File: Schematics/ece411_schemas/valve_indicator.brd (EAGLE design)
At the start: 85.1 x 53.6 mm, 66 parts, among them IC1 STM32F042K6T6, T1 2N2222, T2 2N2222, T3 2N2222, T4 2N2222, U1 DIODES_INC._AZ34063UMTR-G1DIO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, U2 DIODES_INC._AZ34063UMTR-G1DIO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

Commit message: dru added, added attributes
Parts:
- RS_L: device SparkFun-Resistors:0603 -> rcl:R0603
- moved C1_H 10.8 mm to (29.2, 34.9), turned to 180 degrees
- moved RS_L 3.59 mm to (36.8, 29.8)
- moved U2 1.42 mm to (34.9, 40.6)
- moved U1 1.42 mm to (34.9, 34.3)
- moved R1_H 0.63 mm to (40.6, 36.8)
- moved R2_H 0.63 mm to (44.5, 38.7)
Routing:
- net +3V3: track 66.0 -> 71.7 mm
- net N$21: track 50.2 -> 47.4 mm
- net N$17: track 59.3 -> 56.9 mm
- net N$18: track 10.9 -> 8.90 mm
- net N$2: track 10.8 -> 8.91 mm
- net N$1: track 54.5 -> 52.9 mm
- net GND: track 52.7 -> 51.7 mm
- net N$13: track 87.6 -> 86.9 mm
- net N$12: track 46.3 -> 45.5 mm
- net N$11: track 51.1 -> 50.3 mm
- net N$19: track 6.97 -> 6.33 mm

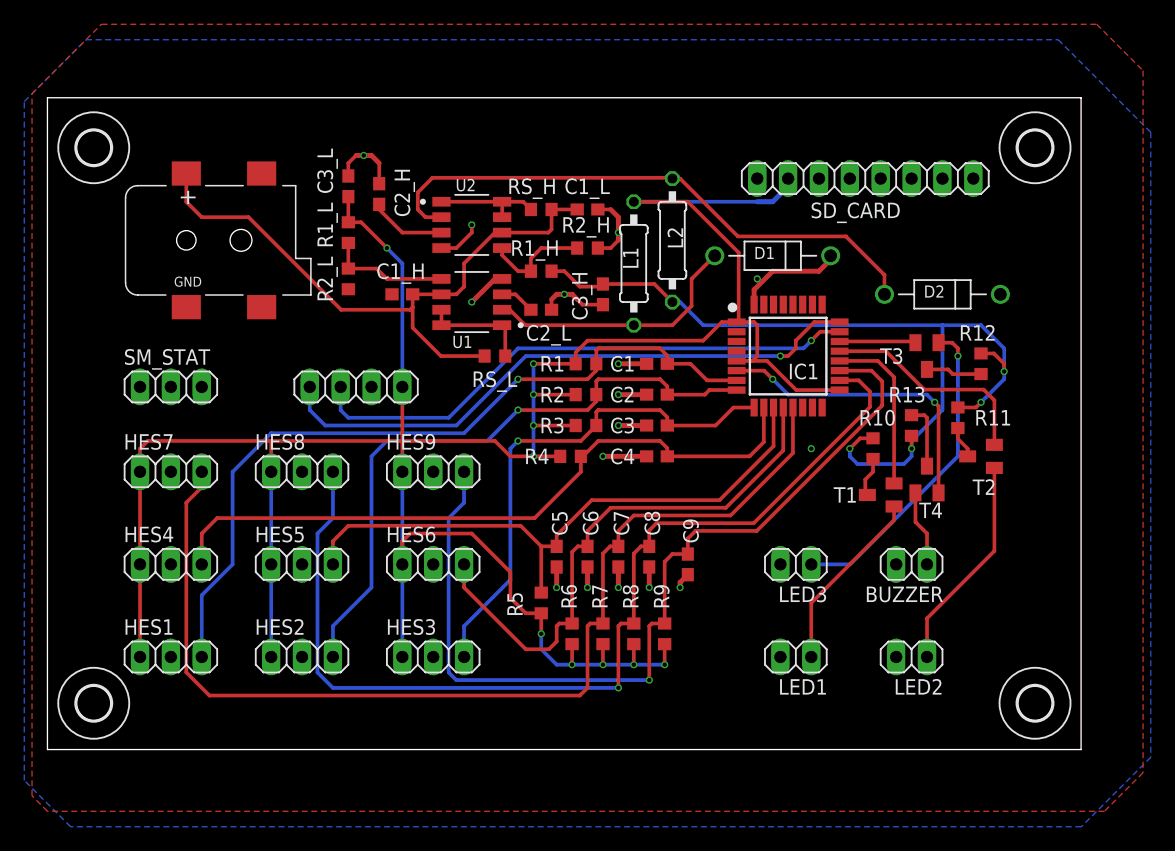
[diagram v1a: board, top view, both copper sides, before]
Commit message: created bom, finished attributes
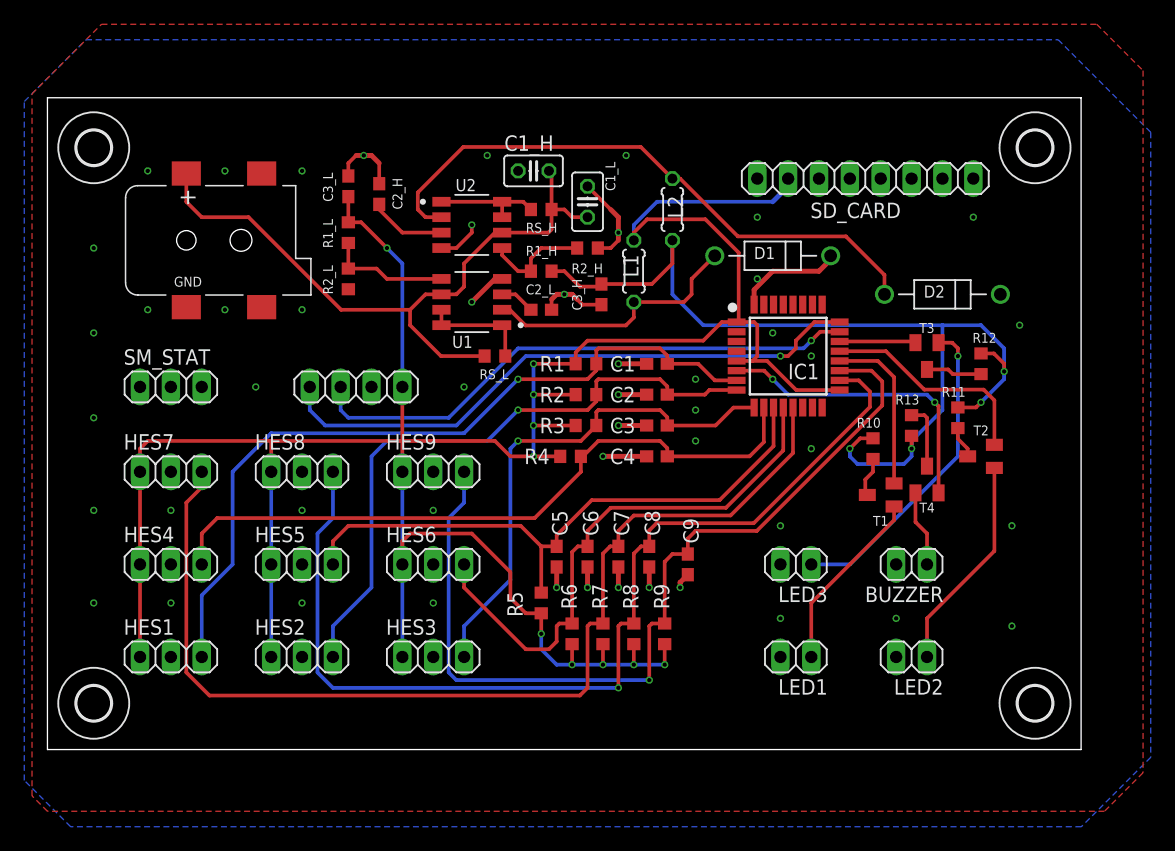
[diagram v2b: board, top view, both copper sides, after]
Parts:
- C1_H, C1_L: device rcl:C0603 -> rcl:C025-025X050
- L1, L2: device eagle-ltspice:0207/10 -> rcl:0204/5
- moved C1_H 14.8 mm to (40.0, 45.1)
- moved L2 2.54 mm to (51.4, 41.9)
- moved C1_L 0.64 mm to (44.5, 42.5), turned to 90 degrees
- moved L1 0.64 mm to (48.3, 36.8)
- moved C3_H 0.13 mm to (45.6, 34.9)
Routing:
- net +3V3: track 71.7 -> 78.4 mm
- net N$1: track 52.9 -> 56.5 mm
- net VCC: track 226.2 -> 228.8 mm
- net N$21: track 47.4 -> 49.5 mm
- net GND: track 51.7 -> 53.2 mm, vias 16 -> 50
